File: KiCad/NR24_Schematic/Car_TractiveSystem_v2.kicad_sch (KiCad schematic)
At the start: 16 parts, among them J1 M_con, J2 F_con, K2 Key Switch Relay, M1 Zero_7R_Motor, SW3 100V E-stop (Right), SW4 100V E-stop (Left), SW7 TI power switch, SW8 GLVMS, U1 Sevcon_Gen4_Size6, U2 Throttle, U4 Vehicle Dynamic Module, U7 Brake Pressure Sensor (Aim)

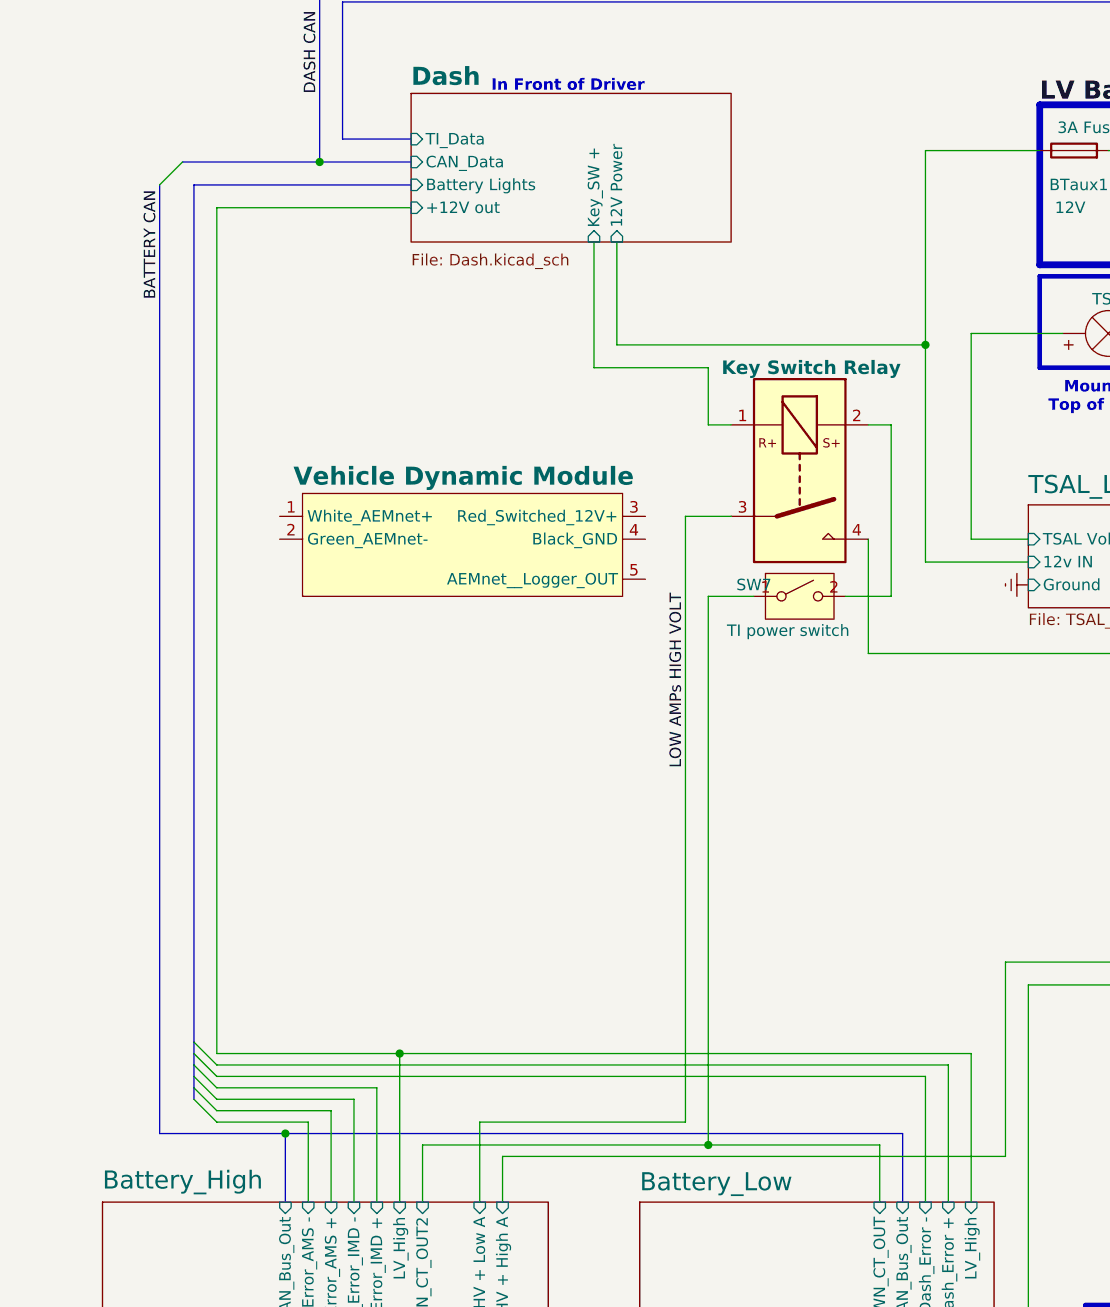
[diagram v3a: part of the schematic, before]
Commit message: Added VDM
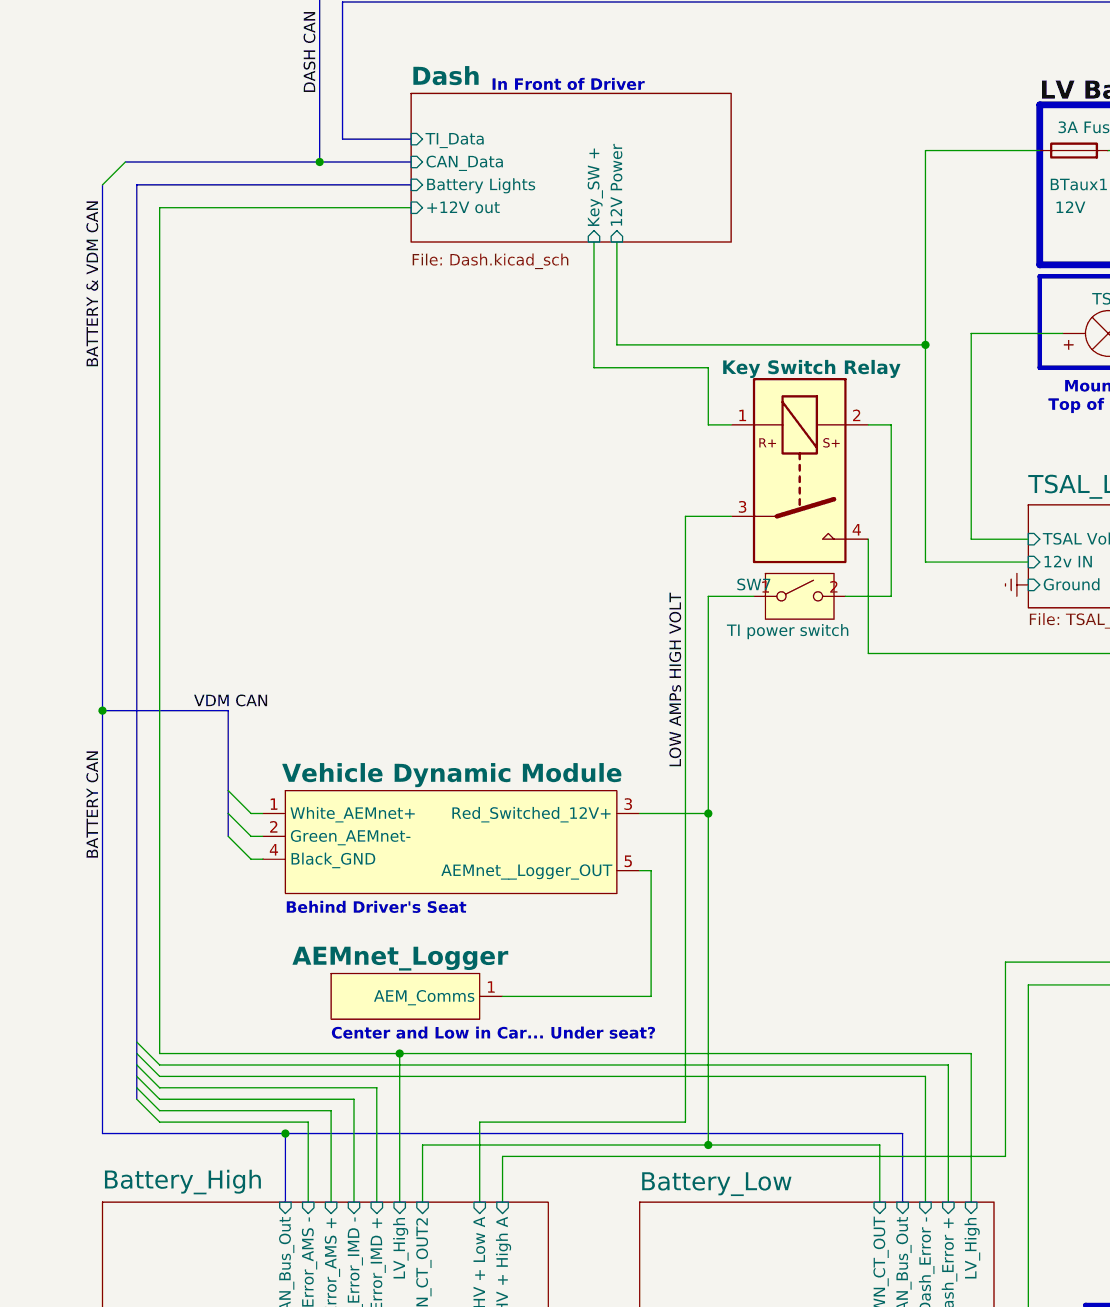
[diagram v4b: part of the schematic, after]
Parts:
- added U6: AEMnet_Logger, symbol CamachosSymbols:Sevcon_Gen4_Size6
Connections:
- net Battery_High/STDWN_CT_OUT2: now also U4.3 (Red_Switched_12V+)
- net at U4.5 (AEMnet__Logger_OUT): now also U6.1 (AEM_Comms)
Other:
- note added: "Behind Driver's Seat"
- note added: "Center and Low in Car... Under seat?"

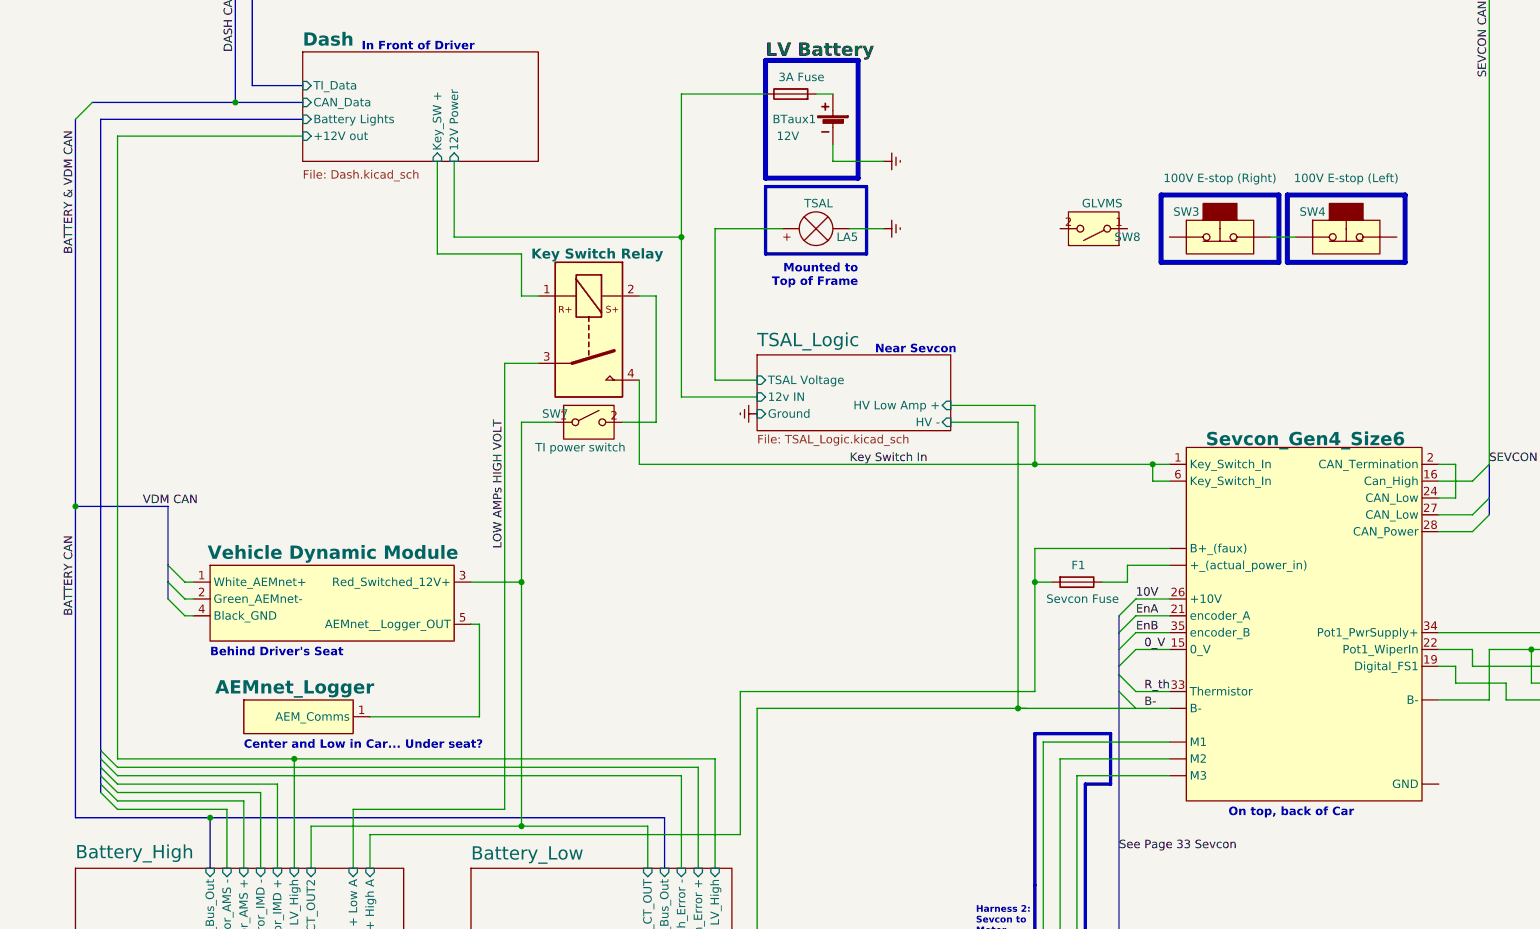
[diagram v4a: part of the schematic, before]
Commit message: Inserted E-Stops
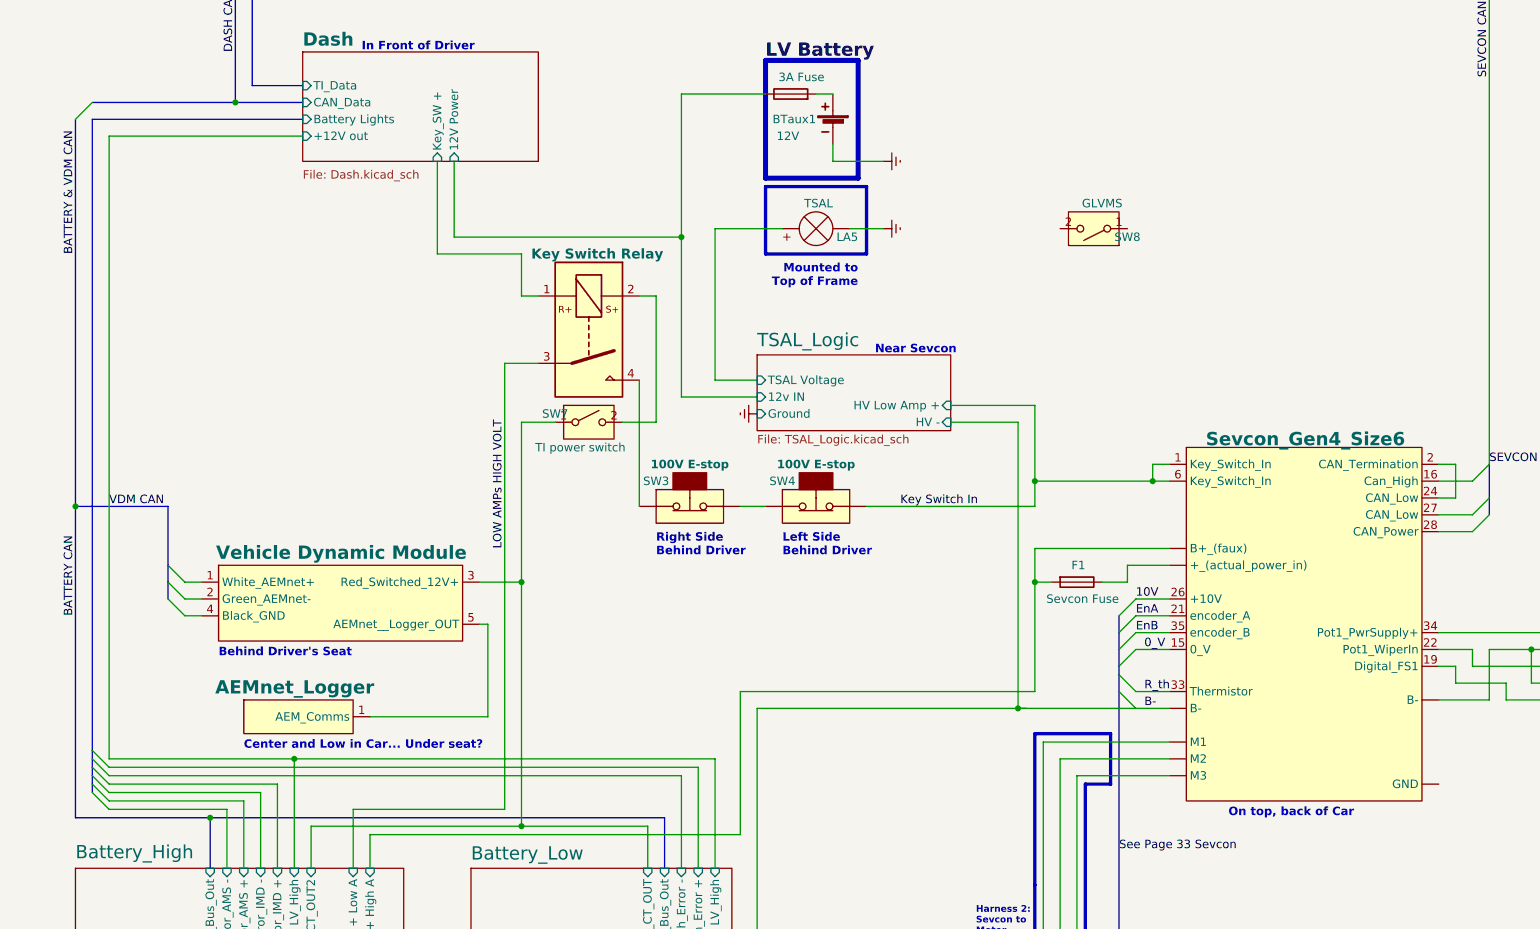
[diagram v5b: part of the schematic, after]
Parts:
- SW3: value 100V E-stop (Right) -> 100V E-stop
- SW4: value 100V E-stop (Left) -> 100V E-stop
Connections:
- net Key Switch In: now also SW4.2 (B); no longer K2.4
- net at SW3.1 (A): now also K2.4
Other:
- note added: "Left Side Behind Driver"
- note added: "Right Side Behind Driver"
- moved on the sheet: SW3, SW4
